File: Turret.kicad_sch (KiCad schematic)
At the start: 19 parts, among them J1 Conn_01x04_Pin, J10 Conn_01x04_Pin, J11 Sabre Vertical Header 6, J12 Conn_01x02_Pin, J2 Conn_01x02_Pin, J20 Conn_01x02_Pin, J21 Conn_01x02_Pin, J3 Conn_01x02_Pin, J4 Conn_01x02_Pin, J5 Conn_01x04_Pin, J6 Conn_01x02_Pin, J7 Conn_01x02_Pin, J8 Conn_01x02_Pin, J9 Conn_01x02_Pin

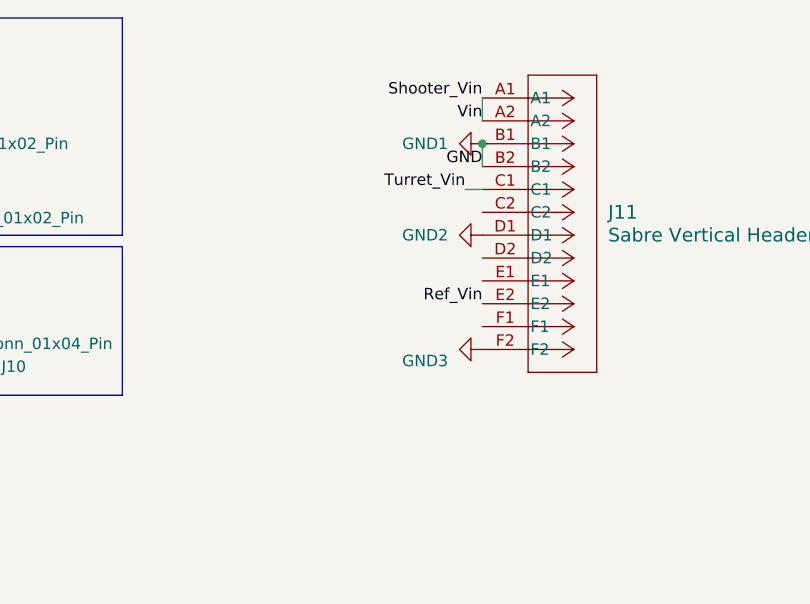
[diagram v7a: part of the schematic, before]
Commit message: fixed gnds on sabre connector
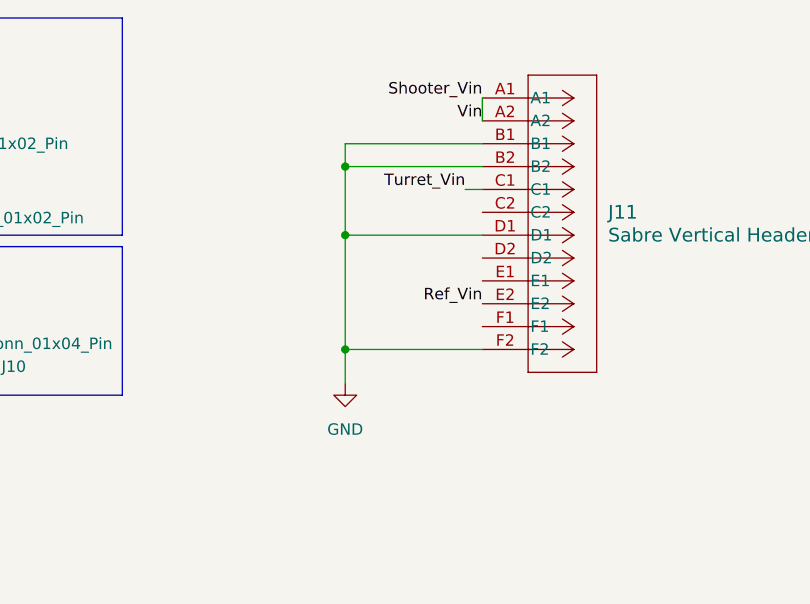
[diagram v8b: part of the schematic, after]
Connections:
- net GND2 is gone; now on net GND: J11.D1
- net GND3 is gone; now on net GND: J11.F2
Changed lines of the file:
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@@
 (kicad_sch (version 20230121) (generator eeschema)
   (paper "A4")
-  (junction (at 182.88 41.275) (diameter 0) (color 0 0 0 0)
+  (junction (at 167.64 64.135) (diameter 0) (color 0 0 0 0)
+  )
+  (junction (at 167.64 51.435) (diameter 0) (color 0 0 0 0)
+  )
+  (junction (at 167.64 43.815) (diameter 0) (color 0 0 0 0)
   )
   (wire (pts (xy 28.575 46.355) (xy 30.48 46.355))
@@
     (stroke (width 0) (type default))
   )
+  (wire (pts (xy 167.64 64.135) (xy 182.88 64.135))
+    (stroke (width 0) (type default))
+  )
   (wire (pts (xy 26.67 41.275) (xy 30.48 41.275))
     (stroke (width 0) (type default))
@@
     (stroke (width 0) (type default))
   )
-  (wire (pts (xy 182.88 41.275) (xy 182.88 43.815))
+  (wire (pts (xy 167.64 41.275) (xy 167.64 43.815))
+    (stroke (width 0) (type default))
+  )
+  (wire (pts (xy 167.64 51.435) (xy 182.88 51.435))
     (stroke (width 0) (type default))
   )
@@
     (stroke (width 0) (type default))
   )
+  (wire (pts (xy 182.88 43.815) (xy 167.64 43.815))
+    (stroke (width 0) (type default))
+  )
+  (wire (pts (xy 167.64 64.135) (xy 167.64 51.435))
+    (stroke (width 0) (type default))
+  )
+  (wire (pts (xy 182.88 41.275) (xy 167.64 41.275))
+    (stroke (width 0) (type default))
+  )
   (wire (pts (xy 109.22 60.96) (xy 120.65 60.96))
     (stroke (width 0) (type default))
@@
     (stroke (width 0) (type default))
   )
+  (wire (pts (xy 167.64 51.435) (xy 167.64 43.815))
+    (stroke (width 0) (type default))
+  )
   (wire (pts (xy 36.195 81.28) (xy 36.195 82.55))
     (stroke (width 0) (type default))
@@
     (stroke (width 0) (type default))
   )
+  (wire (pts (xy 167.64 67.945) (xy 167.64 64.135))
+    (stroke (width 0) (type default))
+  )
   (wire (pts (xy 67.31 36.195) (xy 78.74 36.195))
     (stroke (width 0) (type default))
@@
   )
   (label "UART_TX" (at 36.83 78.74 180) (fields_autoplaced)
-    (effects (font (size 1.27 1.27)) (justify right bottom))
-  )
-  (label "GND" (at 182.88 43.815 180) (fields_autoplaced)
     (effects (font (size 1.27 1.27)) (justify right bottom))
   )
@@
     )
   )
-  (symbol (lib_id "power:GND3") (at 182.88 64.135 270) (unit 1)
-    (in_bom yes) (on_board yes) (dnp no)
-    (property "Reference" "#PWR09" (at 176.53 64.135 0)
-      (effects (font (size 1.27 1.27)) hide)
-    )
-    (property "Value" "GND3" (at 179.07 65.405 90)
-      (effects (font (size 1.27 1.27)) (justify right))
-    )
-    (property "Footprint" "" (at 182.88 64.135 0)
-      (effects (font (size 1.27 1.27)) hide)
-    )
-    (property "Datasheet" "" (at 182.88 64.135 0)
-      (effects (font (size 1.27 1.27)) hide)
-    )
-    (pin "1")
-    (instances
-      (project "Turret"
-        (path "/84905b3c-2997-4e61-b373-c0062fb72371"
-          (reference "#PWR09") (unit 1)
-        )
-      )
-    )
-  )
   (symbol (lib_id "power:+24V") (at 112.395 36.83 0) (unit 1)
     (in_bom yes) (on_board yes) (dnp no) (fields_autoplaced)
@@
     )
   )
-  (symbol (lib_id "power:GND2") (at 182.88 51.435 270) (unit 1)
-    (in_bom yes) (on_board yes) (dnp no) (fields_autoplaced)
-    (property "Reference" "#PWR07" (at 176.53 51.435 0)
-      (effects (font (size 1.27 1.27)) hide)
-    )
-    (property "Value" "GND2" (at 179.07 51.435 90)
-      (effects (font (size 1.27 1.27)) (justify right))
-    )
-    (property "Footprint" "" (at 182.88 51.435 0)
-      (effects (font (size 1.27 1.27)) hide)
-    )
-    (property "Datasheet" "" (at 182.88 51.435 0)
-      (effects (font (size 1.27 1.27)) hide)
-    )
-    (pin "1")
-    (instances
-      (project "Turret"
-        (path "/84905b3c-2997-4e61-b373-c0062fb72371"
-          (reference "#PWR07") (unit 1)
-        )
-      )
-    )
-  )
   (symbol (lib_id "Mechanical:MountingHole") (at 43.815 103.505 0) (unit 1)
     (in_bom yes) (on_board yes) (dnp no) (fields_autoplaced)
@@
     )
   )
-  (symbol (lib_id "power:GND1") (at 182.88 41.275 270) (unit 1)
-    (in_bom yes) (on_board yes) (dnp no) (fields_autoplaced)
-    (property "Reference" "#PWR06" (at 176.53 41.275 0)
-      (effects (font (size 1.27 1.27)) hide)
-    )
-    (property "Value" "GND1" (at 179.07 41.275 90)
-      (effects (font (size 1.27 1.27)) (justify right))
-    )
-    (property "Footprint" "" (at 182.88 41.275 0)
-      (effects (font (size 1.27 1.27)) hide)
-    )
-    (property "Datasheet" "" (at 182.88 41.275 0)
-      (effects (font (size 1.27 1.27)) hide)
-    )
-    (pin "1")
-    (instances
-      (project "Turret"
-        (path "/84905b3c-2997-4e61-b373-c0062fb72371"
-          (reference "#PWR06") (unit 1)
-        )
-      )
+  (symbol (lib_id "power:GND") (at 167.64 67.945 0) (unit 1)
+    (in_bom yes) (on_board yes) (dnp no) (fields_autoplaced)
+    (property "Reference" "#PWR019" (at 167.64 74.295 0)
+      (effects (font (size 1.27 1.27)) hide)
+    )
+    (property "Value" "GND" (at 167.64 73.025 0)
+      (effects (font (size 1.27 1.27)))
+    )
+    (property "Footprint" "" (at 167.64 67.945 0)
+      (effects (font (size 1.27 1.27)) hide)
+    )
+    (property "Datasheet" "" (at 167.64 67.945 0)
+      (effects (font (size 1.27 1.27)) hide)
+    )
+    (pin "1")
+    (instances
+      (project "Turret"
+        (path "/84905b3c-2997-4e61-b373-c0062fb72371"
+          (reference "#PWR019") (unit 1)
+        )
+      )
